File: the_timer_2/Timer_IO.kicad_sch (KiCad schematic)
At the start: 23 parts, among them J1 Screw_Terminal_01x06, J5 R41-B583A, J7 Screw_Terminal_01x02, Q1 AS2312, Q3 AS2312, Q5 AS2312, U13 TPD4S014DSQR

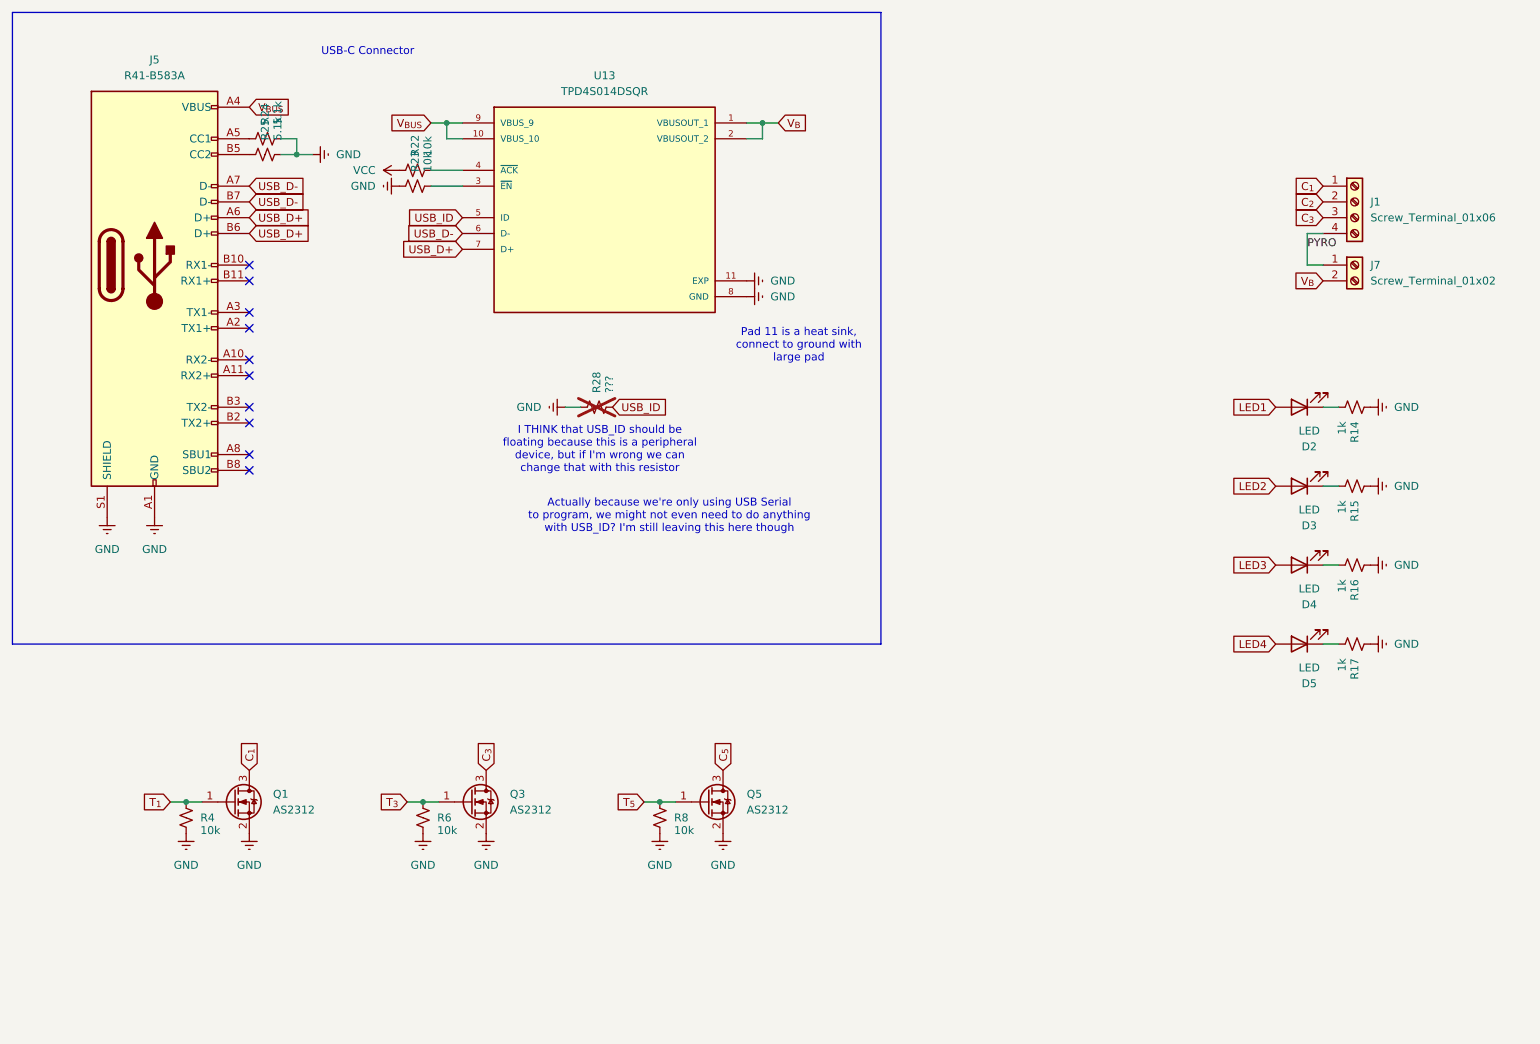
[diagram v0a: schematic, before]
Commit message: Mostly de-exploded the schematic
Also like sorta fixed the PCB design but not really but sorta
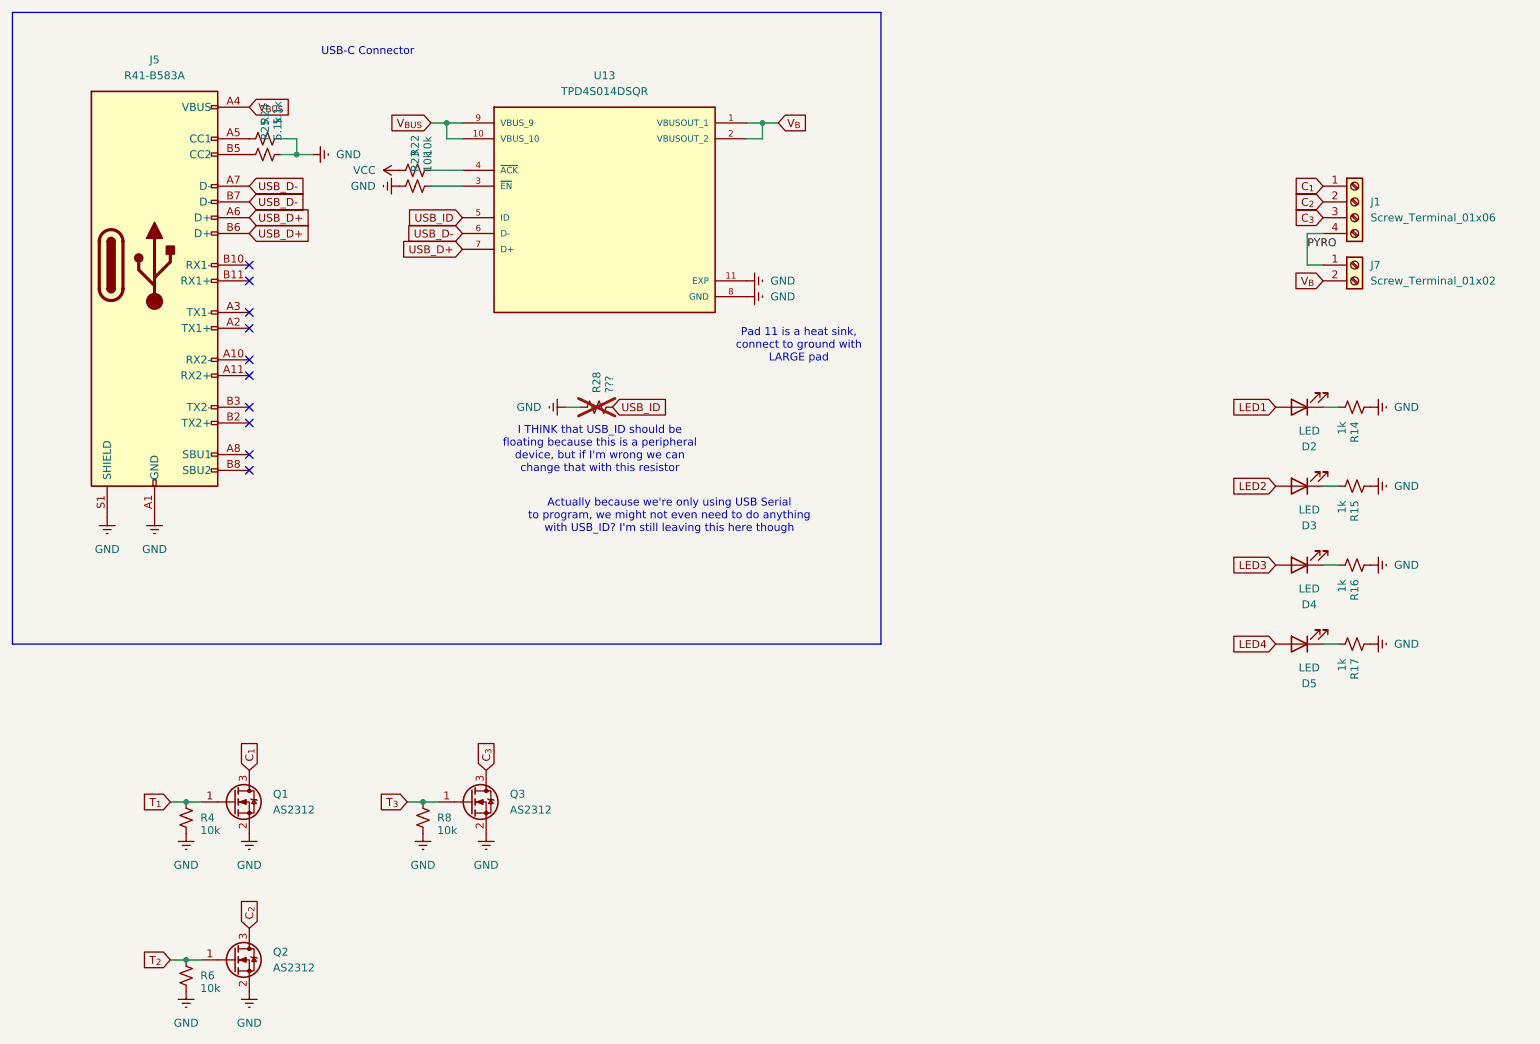
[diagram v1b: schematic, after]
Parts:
- removed Q5: AS2312, Package_TO_SOT_SMD:SOT-23, symbol Transistor_FET:2N7002
- added Q2: AS2312, Package_TO_SOT_SMD:SOT-23, symbol Transistor_FET:2N7002
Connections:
- net T_{5} is gone; now on net T_{3}: R8.1
- net C_{2}: now also Q2.3 (D)
- net GND: now also Q2.2 (S)
- net T_{3}: no longer R6.1
- new net T_{2}: Q2.1 (G), R6.1
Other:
- note added: "Pad 11 is a heat sink, connect to ground with LARGE pad"
- note removed: "Pad 11 is a heat sink, connect to ground with large pad"
